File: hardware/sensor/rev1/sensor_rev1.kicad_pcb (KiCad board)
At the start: 2 copper layers, 100 x 39 mm, 51 parts, among them IC1 STM8L051F3P6, IC2 CC1101RGPR, J1 G8250041000YEU, J2 M20-9770342, Y1 NX3225GA-26.000M-STD-CRG-2

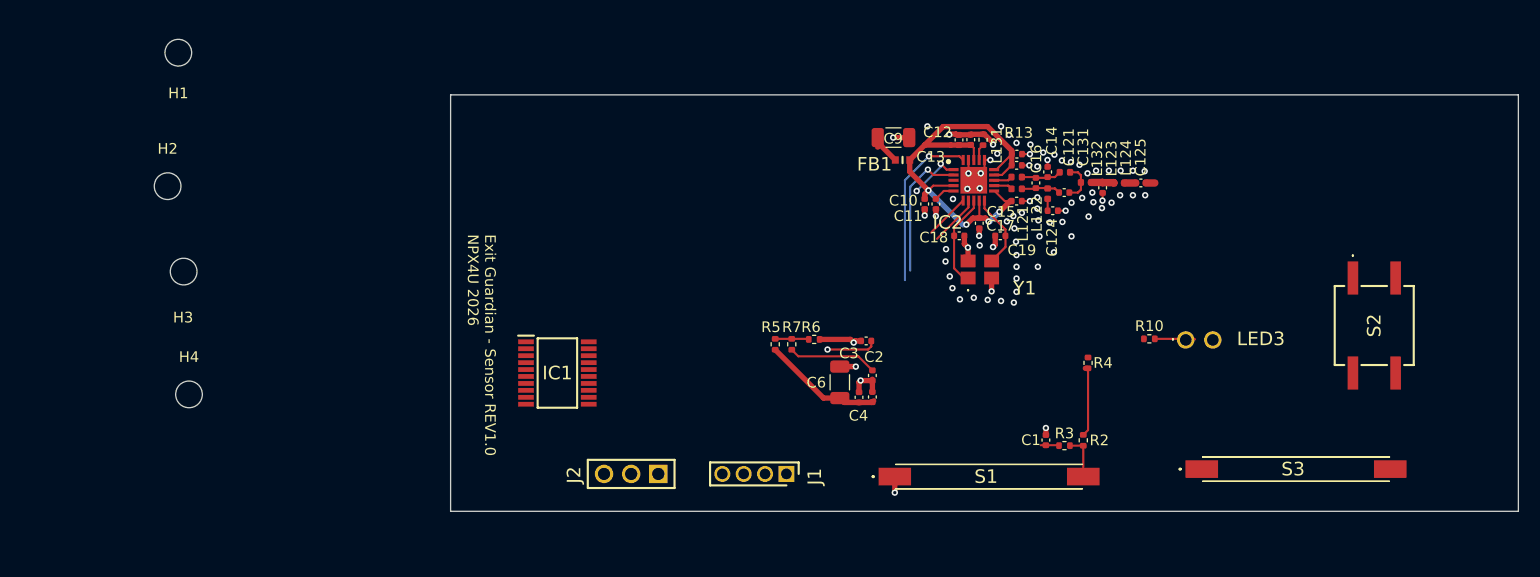
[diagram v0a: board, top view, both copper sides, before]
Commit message: EG-49 Several components addes, such as bulk capacitors, battery holder, MCU and reed switches.
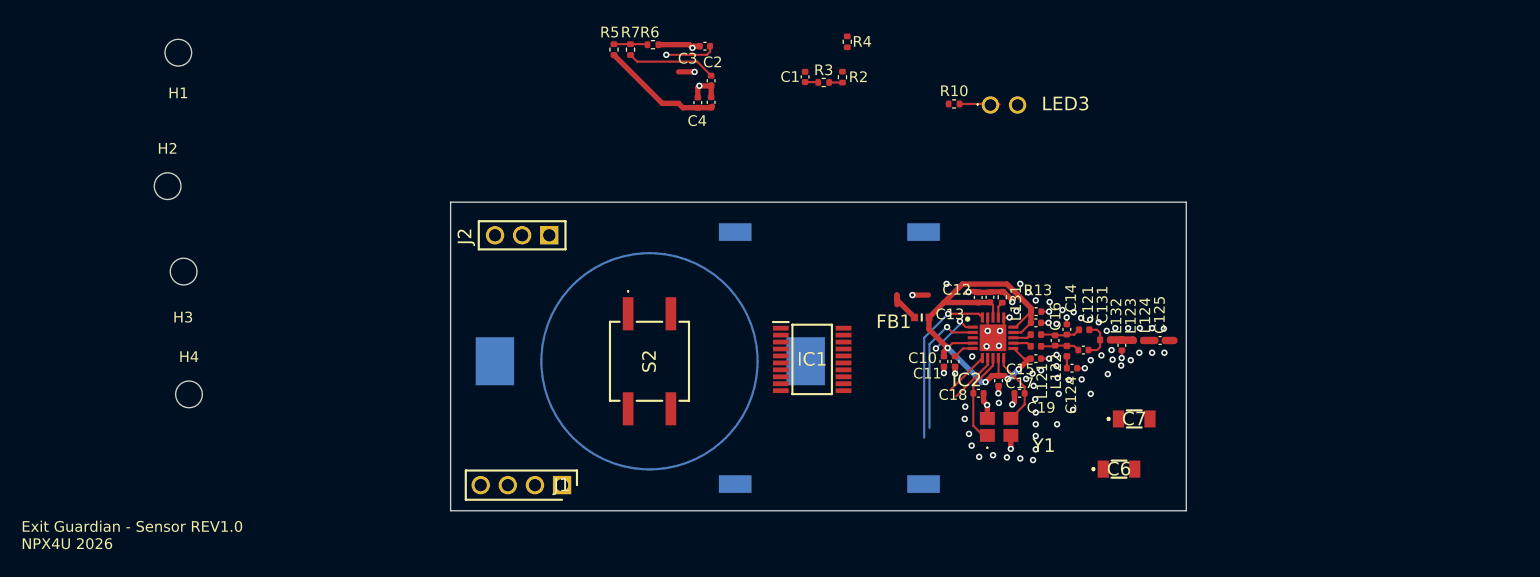
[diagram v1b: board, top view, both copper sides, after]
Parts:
- removed C9: 47uF, 6.3V, Capacitor_SMD:C_1206_3216Metric
- added BT1: BAT-HLD-013-SMT-TR, MyParts:BATHLD013SMTTR, B.Cu at (198.2, 145.9)
- added C7: GRM31CR61A107MEA8L, MyParts:GRM31x, F.Cu at (243.5, 151.3)
- C6: value 47uF, 6.3V -> GRM31CR61A107MEA8L; footprint Capacitor_SMD:C_1206_3216Metric -> MyParts:GRM31x
- J1: value G8250041000YEU -> 22-28-4044; footprint MyParts:HDRV4W55P0X200_1X4_800X200X635P -> MyParts:HDRV4W66P0X254_1X4_1016X249X1067P
- S1, S3: moved to B.Cu
- moved S2 68.0 mm to (198.1, 145.9)
- moved S3 43.7 mm to (215.0, 157.4), turned to 180 degrees
- moved C1 40.8 mm to (212.7, 119.3)
- moved R2 40.8 mm to (216.2, 119.3)
- moved R3 40.8 mm to (214.4, 119.8)
- moved R4 37.6 mm to (216.7, 116.0)
- moved R6 31.5 mm to (198.4, 116.2)
- moved C3 31.5 mm to (203.3, 116.4)
- moved C4 31.5 mm to (202.7, 121.7)
- moved C5 31.5 mm to (203.9, 121.6)
- moved R5 31.5 mm to (194.8, 116.7)
- moved R7 31.5 mm to (196.3, 116.7)
- moved C2 31.5 mm to (203.9, 119.6)
- moved R10 28.6 mm to (226.7, 121.8)
- moved LED3 28.6 mm to (230.1, 121.9)
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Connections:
- C6 pad 1: VDD -> GND
- C6 pad 2: GND -> VDD
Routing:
- net VDD: track 21.9 -> 15.2 mm
- net Net-(R2-Pad1): track 4.14 -> 1.25 mm
- net GND: track 36.9 -> 34.3 mm, vias 82 -> 80
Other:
- board size 100 x 39 mm -> 68.9 x 28.9 mm
